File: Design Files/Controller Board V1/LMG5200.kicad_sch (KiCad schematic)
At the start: 4 parts, among them Q1 LMG5200

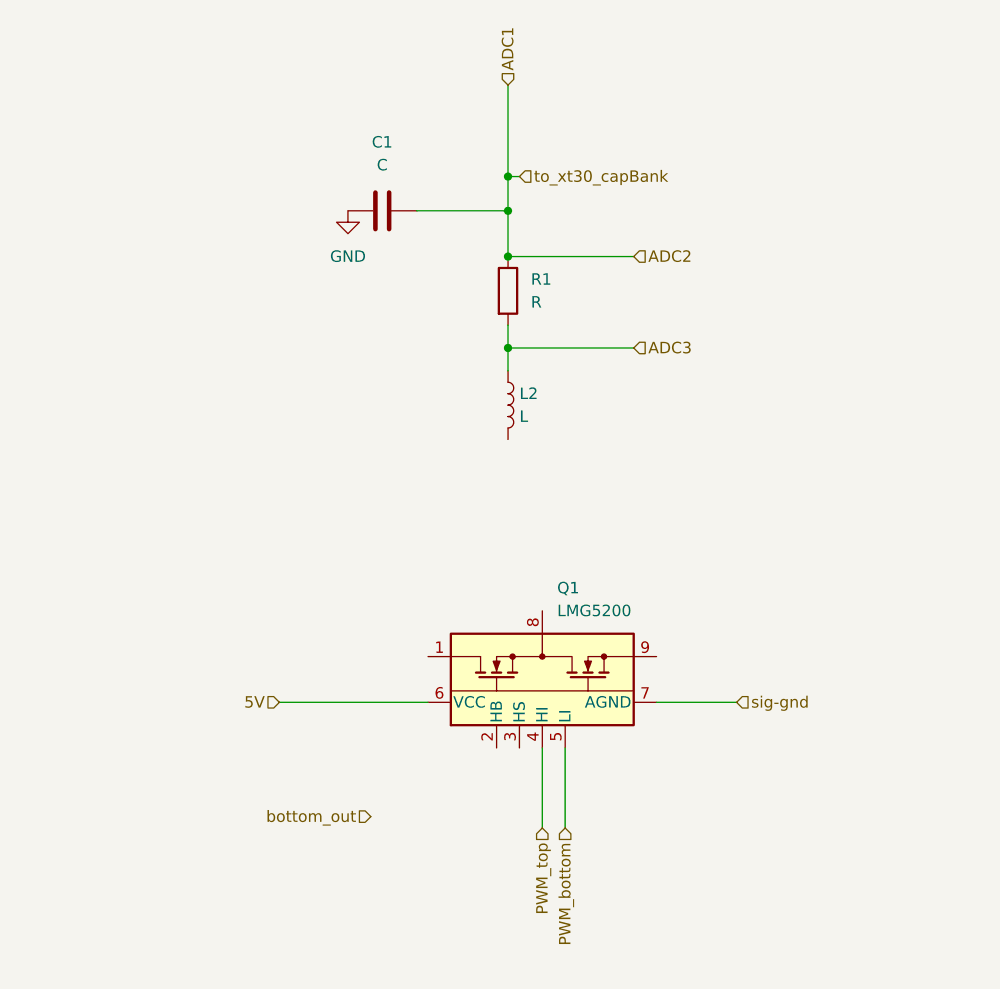
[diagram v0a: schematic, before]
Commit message: small tweaks to half bridge schematic
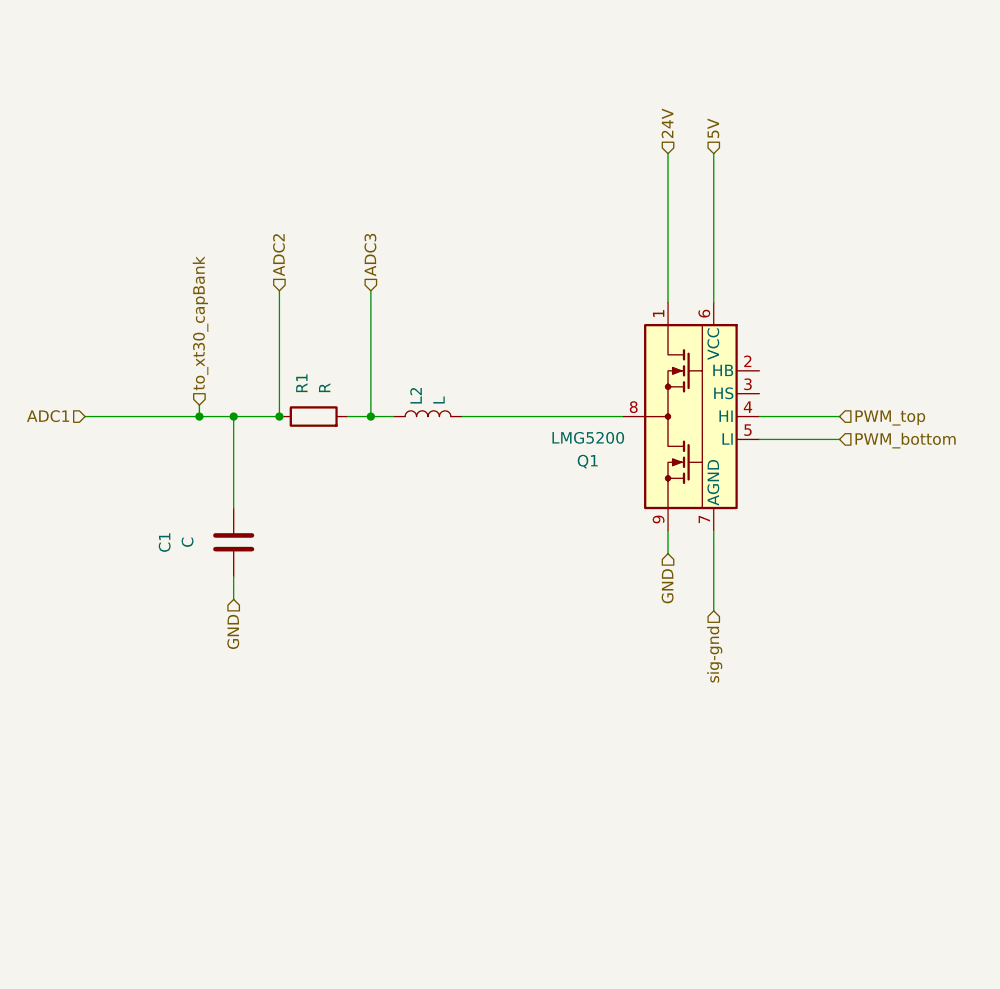
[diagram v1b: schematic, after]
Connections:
- net GND: now also Q1.9
- net at L2.2: now also Q1.8
- net 24V: now reaches Q1.1
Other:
- moved on the sheet: C1, L2, Q1, R1
